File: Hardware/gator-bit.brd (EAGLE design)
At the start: 114.4 x 70.4 mm, 90 parts, among them J1 GATOR, J10 GATOR, J11 GATOR, J12 GATOR, J13 GATOR, J14 GATOR, J15 GATOR, J16 GATOR, J17 GATOR, J18 GATOR, J2 GATOR, J3 GATOR, J4 GATOR, J6 GATOR, J7 GATOR, J8 GATOR, J9 GATOR, U1 TPS63070, U2 micro:bit, U3 V_REG_MIC52053.0V, U4 GATORBIT_LM317

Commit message: Updated parts with SKUs
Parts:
- C9: value 47uF -> 47UF
- L1: value XFL4020 -> 1.5UH
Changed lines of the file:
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@@
 <attribute name="PROD_ID" value="CAP-00810" x="90.17" y="27.6225" size="1.778" layer="27" rot="R270" display="off"/>
 </element>
-<element name="C9" library="SparkFun-Capacitors" package="0805" value="47uF" x="92.71" y="33.3375" rot="R90">
-<attribute name="PROD_ID" value="" x="92.71" y="33.3375" size="1.778" layer="27" rot="R90" display="off"/>
+<element name="C9" library="SparkFun-Capacitors" package="0805" value="47UF" x="92.71" y="33.3375" rot="R90">
+<attribute name="PROD_ID" value="CAP-13854" x="92.71" y="33.3375" size="1.778" layer="27" rot="R90" display="off"/>
 </element>
-<element name="L1" library="SparkFun-Coils" package="XFL4020" value="XFL4020" x="89.37625" y="37.465" rot="R180"/>
+<element name="L1" library="SparkFun-Coils" package="XFL4020" value="1.5UH" x="89.37625" y="37.465" rot="R180">
+<attribute name="PROD_ID" value="NDUC-13855" x="89.37625" y="37.465" size="1.778" layer="27" rot="R180" display="off"/>
+<attribute name="VALUE" value="1.5UH" x="89.37625" y="37.465" size="1.778" layer="27" rot="R180" display="off"/>
+</element>
 <element name="U3" library="SparkFun-IC-Power" package="SOT23-5" value="V_REG_MIC52053.0V" x="88.07564375" y="53.77528125"/>
 <element name="C10" library="SparkFun-Capacitors" package="0603" value="0.1uF" x="88.9" y="60.6425" rot="R180">

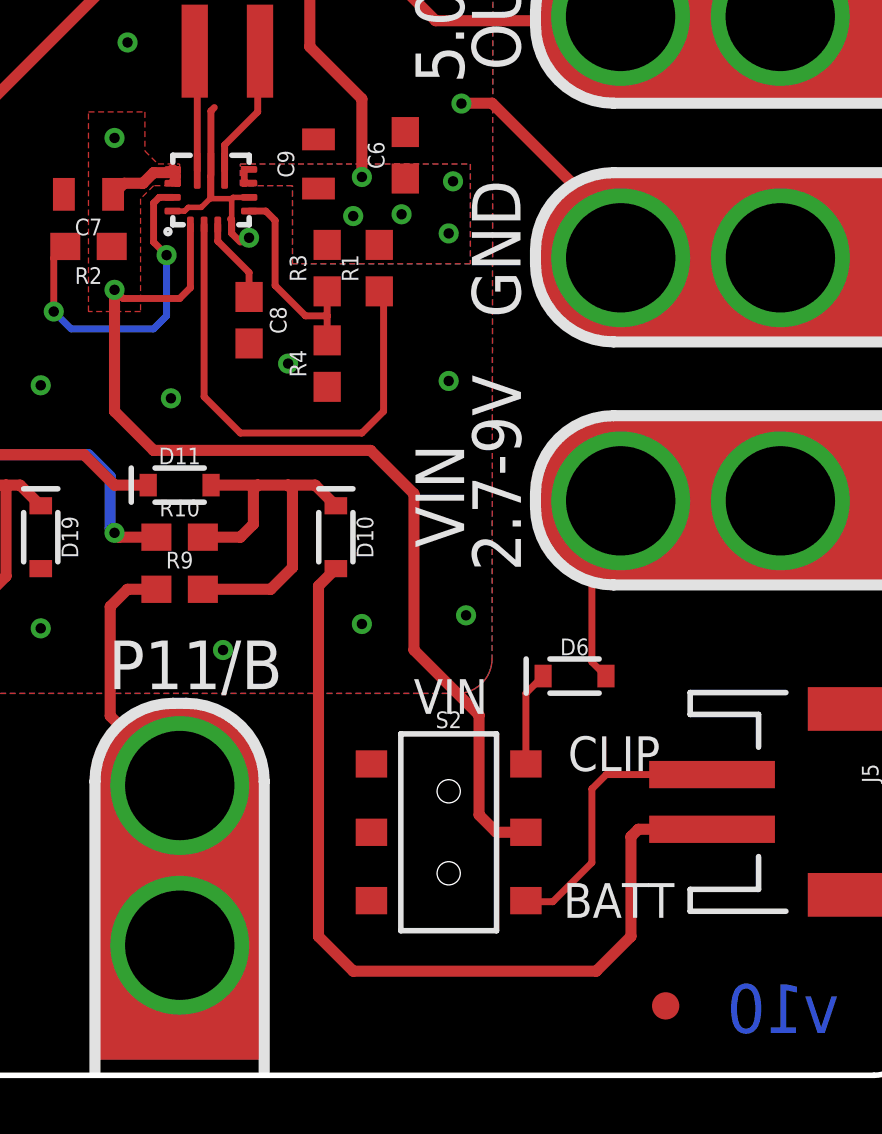
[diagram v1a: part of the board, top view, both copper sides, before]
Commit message: updating Buck-Boost part
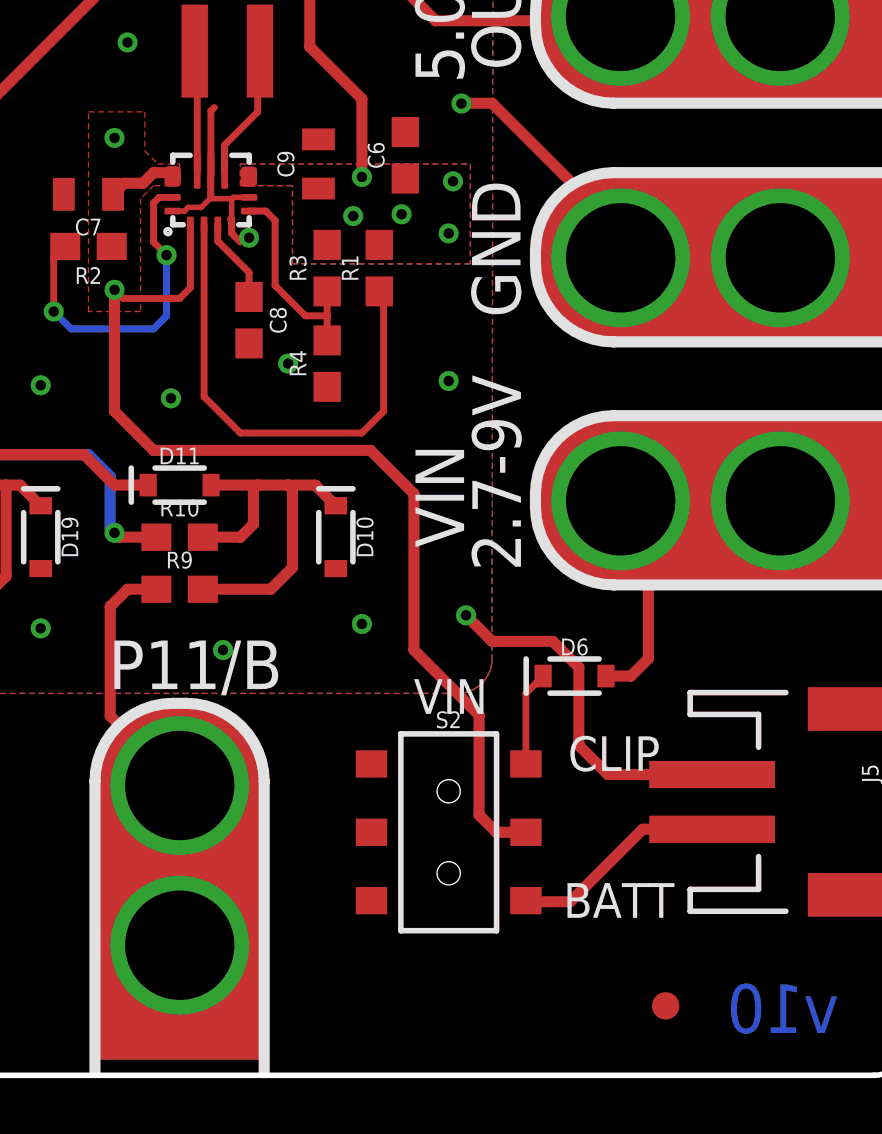
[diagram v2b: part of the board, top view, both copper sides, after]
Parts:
- U4: value GATORBIT_LM317 -> ADJ REG 1.5A
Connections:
- net 5V: no longer U1.P$78, U1.P$8
- net GND: now also J5.1; no longer J5.2
- net VIN: no longer U1.P$1213, U1.P$13
- net V_BATT: now also J5.2; no longer J5.1
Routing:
- net GND: track 88.6 -> 68.8 mm
- net V_BATT: track 10.3 -> 7.92 mm
- net VIN_TAB: track 12.9 -> 13.8 mm

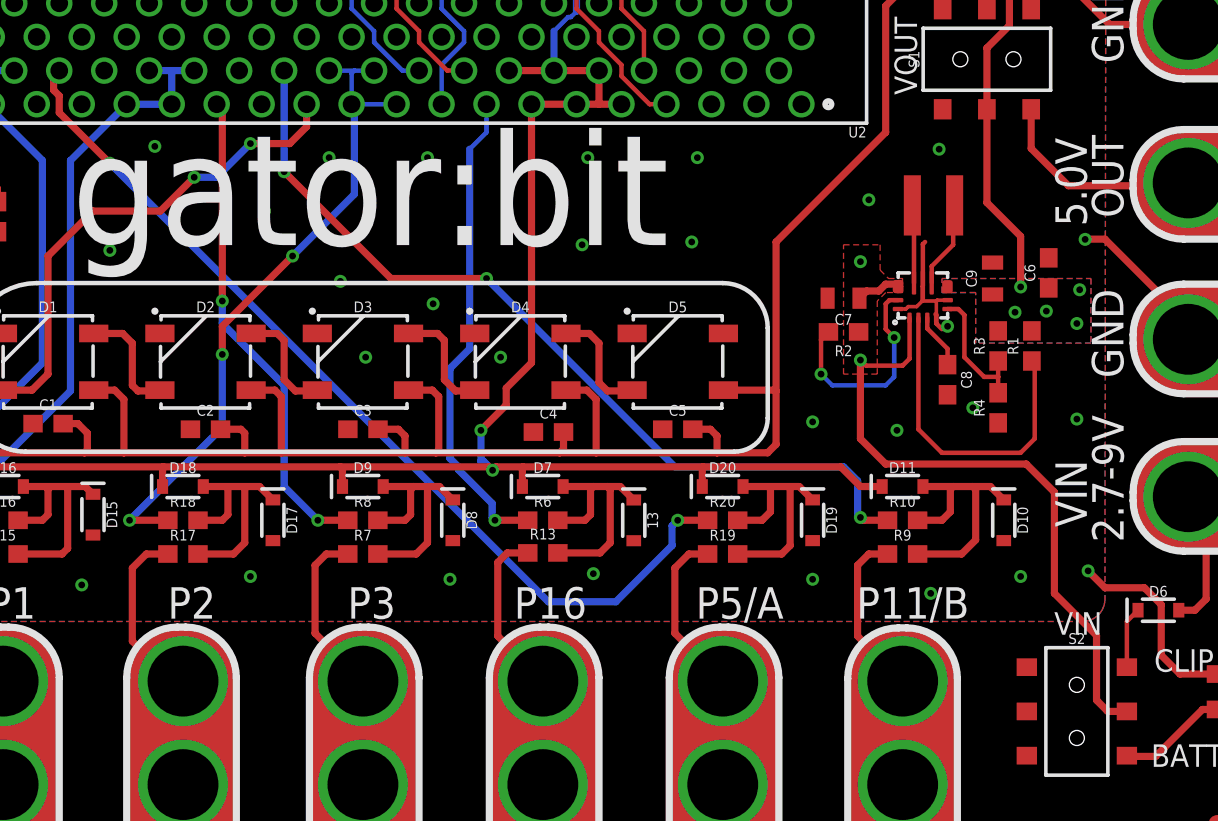
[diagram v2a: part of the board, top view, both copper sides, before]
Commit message: Fixing ground pour
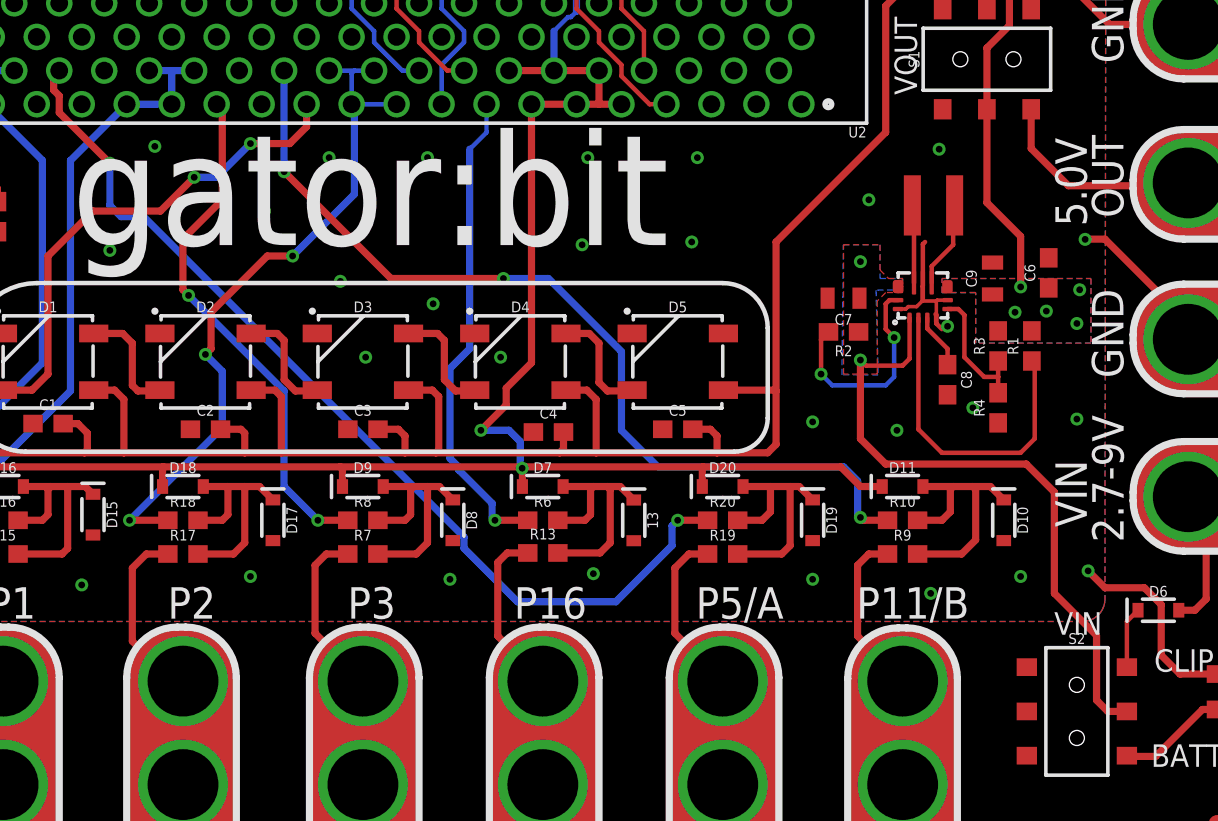
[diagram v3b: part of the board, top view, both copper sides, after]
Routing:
- net VIN: track 40.1 -> 37.3 mm
- net P11: track 49.1 -> 51.7 mm
- net P8: track 27.6 -> 29.4 mm
- net P5: track 53.3 -> 55.0 mm
- net P2: track 38.0 -> 39.6 mm
- net 3.0V: track 148.4 -> 149.7 mm
- added copper zone on layer 16, net VIN

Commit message: Updates Per QC Review
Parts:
- moved LOGO4 143.0 mm to (73.5, 15.4)
- renumbered 13 to D13
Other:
- board text added: "v01"
- board text removed: "v10"

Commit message: Updating VREG 3.0V Package
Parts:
- U3: value V_REG_MIC52053.0V -> MIC52053.0V
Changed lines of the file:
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@@
 <attribute name="VALUE" value="1.5UH" x="89.37625" y="37.465" size="1.778" layer="27" rot="R180" display="off"/>
 </element>
-<element name="U3" library="SparkFun-IC-Power" package="SOT23-5" value="V_REG_MIC52053.0V" x="88.07564375" y="53.77528125"/>
+<element name="U3" library="SparkFun-IC-Power" package="SOT23-5" value="MIC52053.0V" x="88.07564375" y="53.77528125">
+<attribute name="VALUE" value="MIC52053.0V" x="88.07564375" y="53.77528125" size="1.778" layer="27" display="off"/>
+<attribute name="PROD_ID" value="VREG-13859" x="88.07564375" y="53.77528125" size="1.778" layer="27" display="off"/>
+</element>
 <element name="C10" library="SparkFun-Capacitors" package="0603" value="0.1uF" x="88.9" y="60.6425" rot="R180">
 <attribute name="PROD_ID" value="CAP-00810" x="88.9" y="60.6425" size="1.778" layer="27" rot="R180" display="off"/>

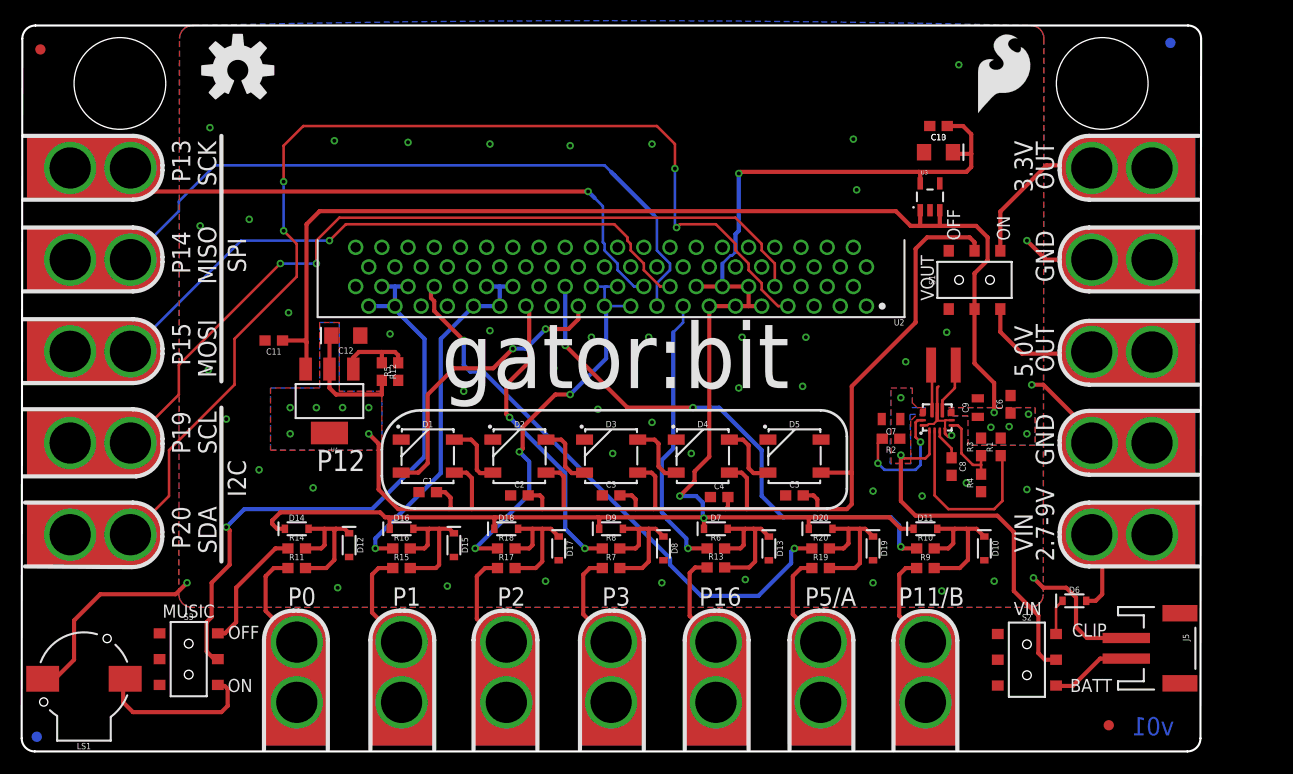
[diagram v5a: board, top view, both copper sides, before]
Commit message: -Updated protection diodes -added a power path to be powered from the micro:bit -added master switch -added status LEDs
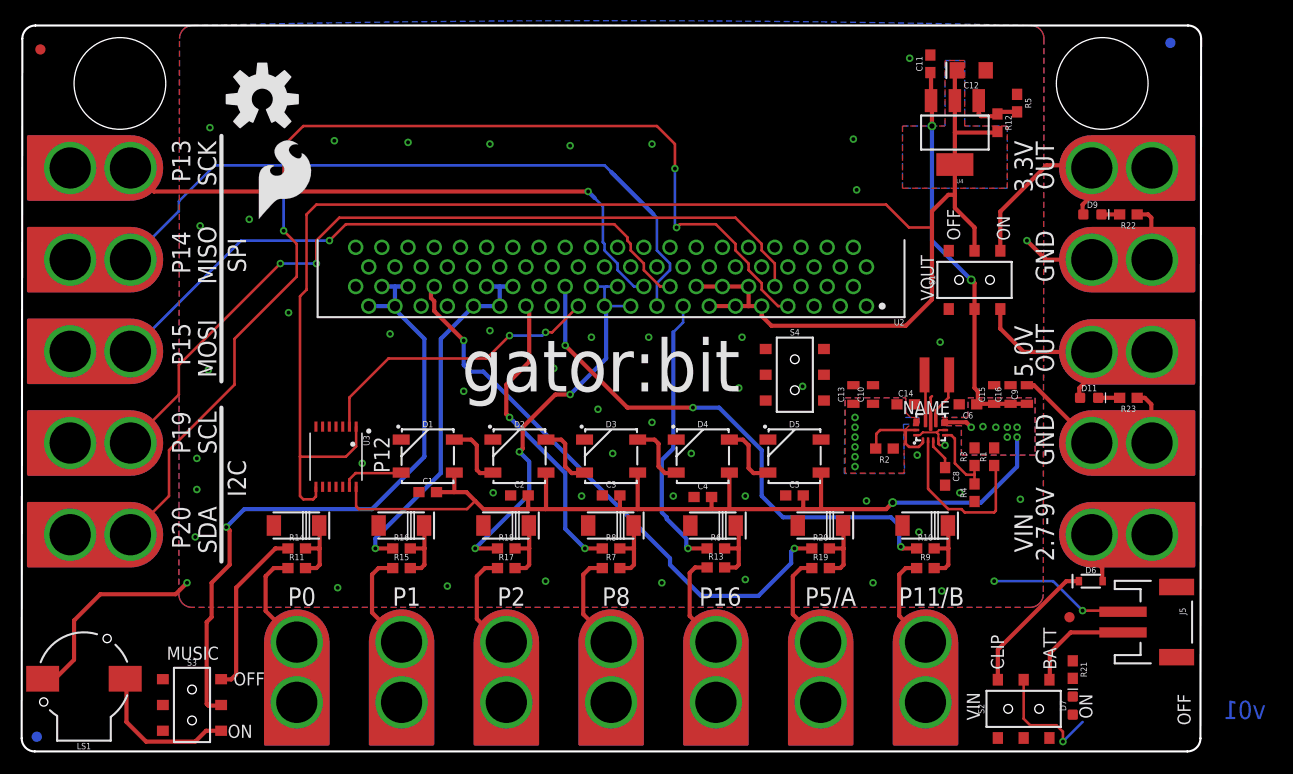
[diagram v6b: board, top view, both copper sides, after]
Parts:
- removed C7: 33UF, SparkFun-Capacitors:0805
- removed D14, D16, D18, D20: 3.3V, SparkFun-DiscreteSemi:SOD-323
- added C14: 10uF, SparkFun-Capacitors:0603
- added C15, C16: 22uF, SparkFun-Capacitors:0805
- added R21, R22, R23: 1k, SparkFun-Resistors:0603
- added S4: (no value), SparkFun-Switches:SWITCH_DPDT_SMD_AYZ0202
- C10: value 0.1uF -> 10uF; device SparkFun-Capacitors:0603 -> SparkFun-Capacitors:0805
- C13: device SparkFun-Capacitors:EIA3216 -> SparkFun-Capacitors:0805
- C9: value 47UF -> 22uF
- D10, D12, D13, D15, D17, D19, D8: value 3.3V -> 3.8V; device SparkFun-DiscreteSemi:SOD-323 -> PDZVTR36BCT:SOD-128
- D11, D7, D9: value 3.3V -> RED; device SparkFun-DiscreteSemi:SOD-323 -> SparkFun-LED:LED-0603
- U3: value MIC52053.0V -> TXB0104; device SparkFun-IC-Power:SOT23-5 -> SparkFun-IC-Comms:TSSOP14
- moved LOGO5 70.5 mm to (22.5, 51.5)
- moved C11 69.1 mm to (88.1, 66.7), turned to 90 degrees
- moved U4 66.0 mm to (90.5, 60.0)
- moved C12 65.9 mm to (92.1, 66.0)
- moved R5 65.4 mm to (96.5, 62.9), turned to 270 degrees
- moved R12 64.4 mm to (94.6, 61.0)
- moved U3 62.9 mm to (30.5, 28.6), turned to 180 degrees
- moved D9 55.7 mm to (103.8, 52.1)
- moved D7 38.6 mm to (101.9, 4.45), turned to 90 degrees
- moved C10 26.8 mm to (82.5, 34.6), turned to 90 degrees
- moved C13 24.9 mm to (80.6, 34.6), turned to 90 degrees
- moved D11 20.3 mm to (103.5, 34.3)
- moved FD3 11.1 mm to (101.6, 13.0)
- moved D10 6.43 mm to (87.3, 21.9)
- moved D13 6.13 mm to (66.7, 21.9)
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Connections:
- removed net 3.0V: C10.1, C13.+, D11.C, D14.C, D16.C, D18.C, D20.C, D7.C, D9.C, U2.A10, U2.A11, U2.A12, U2.A13, U2.A14, U2.A9, U3.5
- new net N$23: D9.C, R22.2
- new net N$24: D11.C, R23.2
- new net N$9: D7.C, R21.2
- new net P12LL: U2.A23, U3.2
- new net VSUPPLY: S2.2, S4.2
- net 3.3V: now also U2.A10, U2.A11, U2.A12, U2.A13, U2.A14, U2.A9, U3.1, U3.8; no longer C1.2, C2.2, C3.2, C4.2, C5.2, D1.1, D2.1, D3.1, D4.1, D5.1
- net 5V: now also C1.2, C15.1, C16.1, C2.2, C3.2, C4.2, C5.2, D1.1, D2.1, D3.1, D4.1, D5.1, U3.14; no longer U3.1, U3.3
- net GND: now also C13.2, C14.2, C15.2, C16.2, D10.P$2, D12.P$2, D13.P$2, D15.P$2, D17.P$2, D19.P$2, D8.P$2, R21.1, R22.1, R23.1, U3.7; no longer C13.-, C7.2, D10.A, D12.A, D13.A, D15.A, D17.A, D19.A, D8.A, U3.2
- net N$13: now also U1.P$1
- net P12: now also U3.13; no longer U2.A23
- net PP0: now also D12.P$1; no longer D12.C, D14.A
- net PP1: now also D15.P$1; no longer D15.C, D16.A
- net PP11: now also D10.P$1; no longer D10.C, D11.A
- net PP16: now also D13.P$1; no longer D13.C, D7.A
- net PP2: now also D17.P$1; no longer D17.C, D18.A
- net PP5: now also D19.P$1; no longer D19.C, D20.A
- net PP8: now also D8.P$1; no longer D8.C, D9.A
- net VIN: now also C10.1, C13.1, C14.1, D7.A, S4.3; no longer C7.1, S2.2, U1.P$1
- net VOUT3.3: now also D9.A
- net VOUT5.0: now also D11.A
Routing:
- net 3.0V: track 149.7 -> 0.00 mm, vias 3 -> 0
- net VIN: track 37.3 -> 0.57 mm, vias 2 -> 6
- net 5V: track 105.5 -> 138.6 mm, vias 5 -> 10
- net 3.3V: track 133.8 -> 165.0 mm, vias 6 -> 0
- net P12LL: track 0.00 -> 28.7 mm, vias 0 -> 2
- net P12: track 28.5 -> 6.01 mm, vias 2 -> 0
- net VSUPPLY: track 0.00 -> 11.8 mm, vias 0 -> 1
- net GND: track 68.8 -> 79.5 mm, vias 49 -> 52
- net N$20: track 3.48 -> 13.5 mm
- net PP11: track 15.1 -> 6.70 mm
- net PP16: track 14.4 -> 6.77 mm
- net PP5: track 14.2 -> 6.70 mm
- net PP8: track 14.1 -> 6.70 mm
- net PP1: track 14.0 -> 6.70 mm
- net PP0: track 13.9 -> 6.70 mm
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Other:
- board text added: "P8"
- board text removed: "P3"

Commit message: -Added Fuse to 3.3V input on the m:b -added silk to show users the sequence of switches -added option to choose powering from m:b (USB) or from an external power supply.
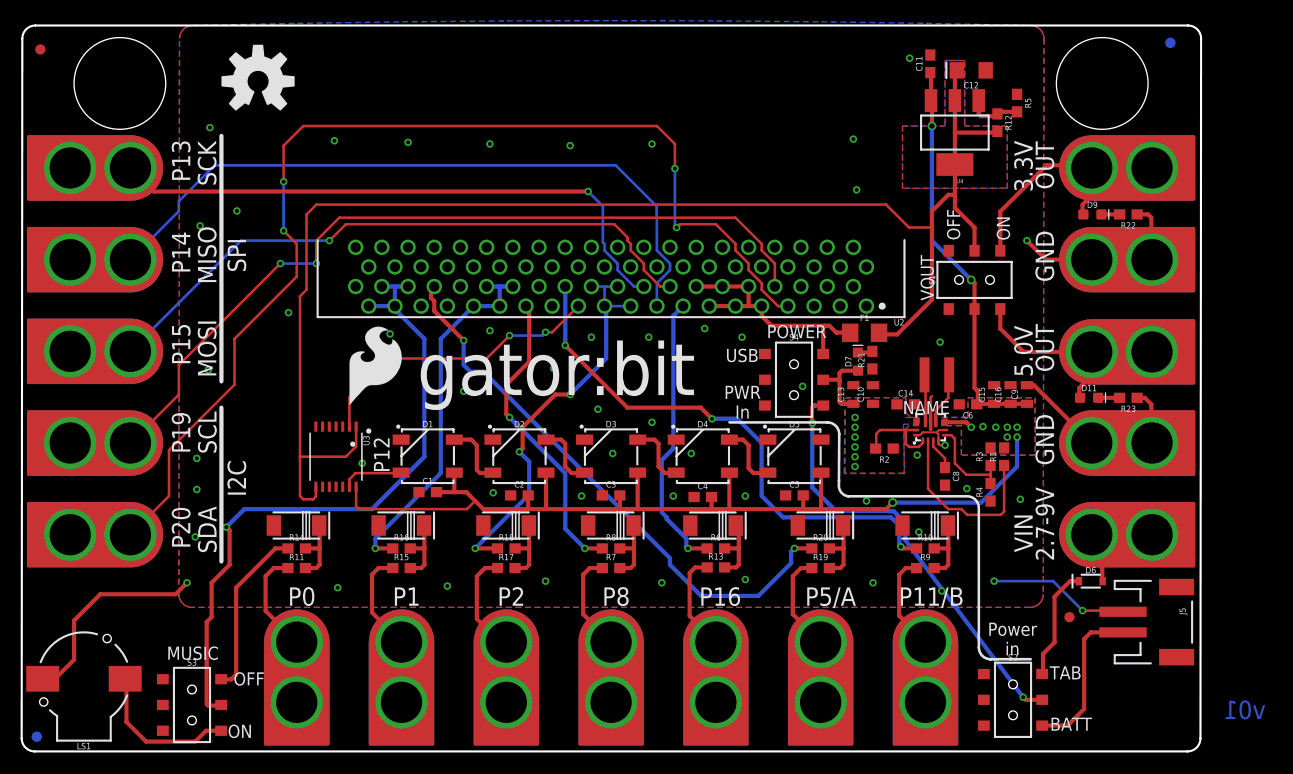
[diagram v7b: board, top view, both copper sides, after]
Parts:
- added F1: 6V/0.5A, SparkFun-Fuses:1206
- moved D7 39.3 mm to (81.1, 37.8)
- moved R21 35.7 mm to (82.5, 37.9), turned to 90 degrees
- moved LOGO5 20.1 mm to (31.3, 33.4)
- moved LOGO6 1.77 mm to (22.9, 65.0)
- moved R4 1.55 mm to (93.9, 25.1)
- moved R3 1.55 mm to (93.9, 28.6)
- moved S2 1.35 mm to (96.1, 5.00), turned to 270 degrees
- moved R1 0.97 mm to (95.3, 28.6)
- moved S4 0.49 mm to (74.9, 36.0)
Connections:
- new net MBIN: F1.1, S4.1, U2.A10, U2.A11, U2.A12, U2.A13, U2.A14, U2.A9
- net 3.3V: now also F1.2; no longer U2.A10, U2.A11, U2.A12, U2.A13, U2.A14, U2.A9
- net VIN: now also S4.2; no longer S4.3
- net VSUPPLY: now also S4.3; no longer S4.2
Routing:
- net VSUPPLY: track 11.8 -> 42.0 mm, vias 1 -> 2
- net MBIN: track 0.00 -> 25.1 mm
- net 3.3V: track 165.0 -> 140.6 mm
- net VIN: track 0.57 -> 8.27 mm
- net V_BATT: track 10.5 -> 15.6 mm
- net N$20: track 13.5 -> 11.0 mm
- net N$11: track 7.63 -> 9.18 mm
- net N$9: track 0.00 -> 1.44 mm
- net N$14: track 16.7 -> 17.7 mm
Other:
- board text added: "POWER"
- board text added: "PWR In"
- board text added: "Power in"
- board text added: "TAB"
- board text added: "USB"
- board text removed: "CLIP"
